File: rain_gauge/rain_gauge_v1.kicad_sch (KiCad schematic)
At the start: 16 parts, among them J1 Conn_01x05_Pin, SW1 SW_Reed, U1 S35770, U2 SN74LVC1G14DBV, U3 AP2112K-3.3

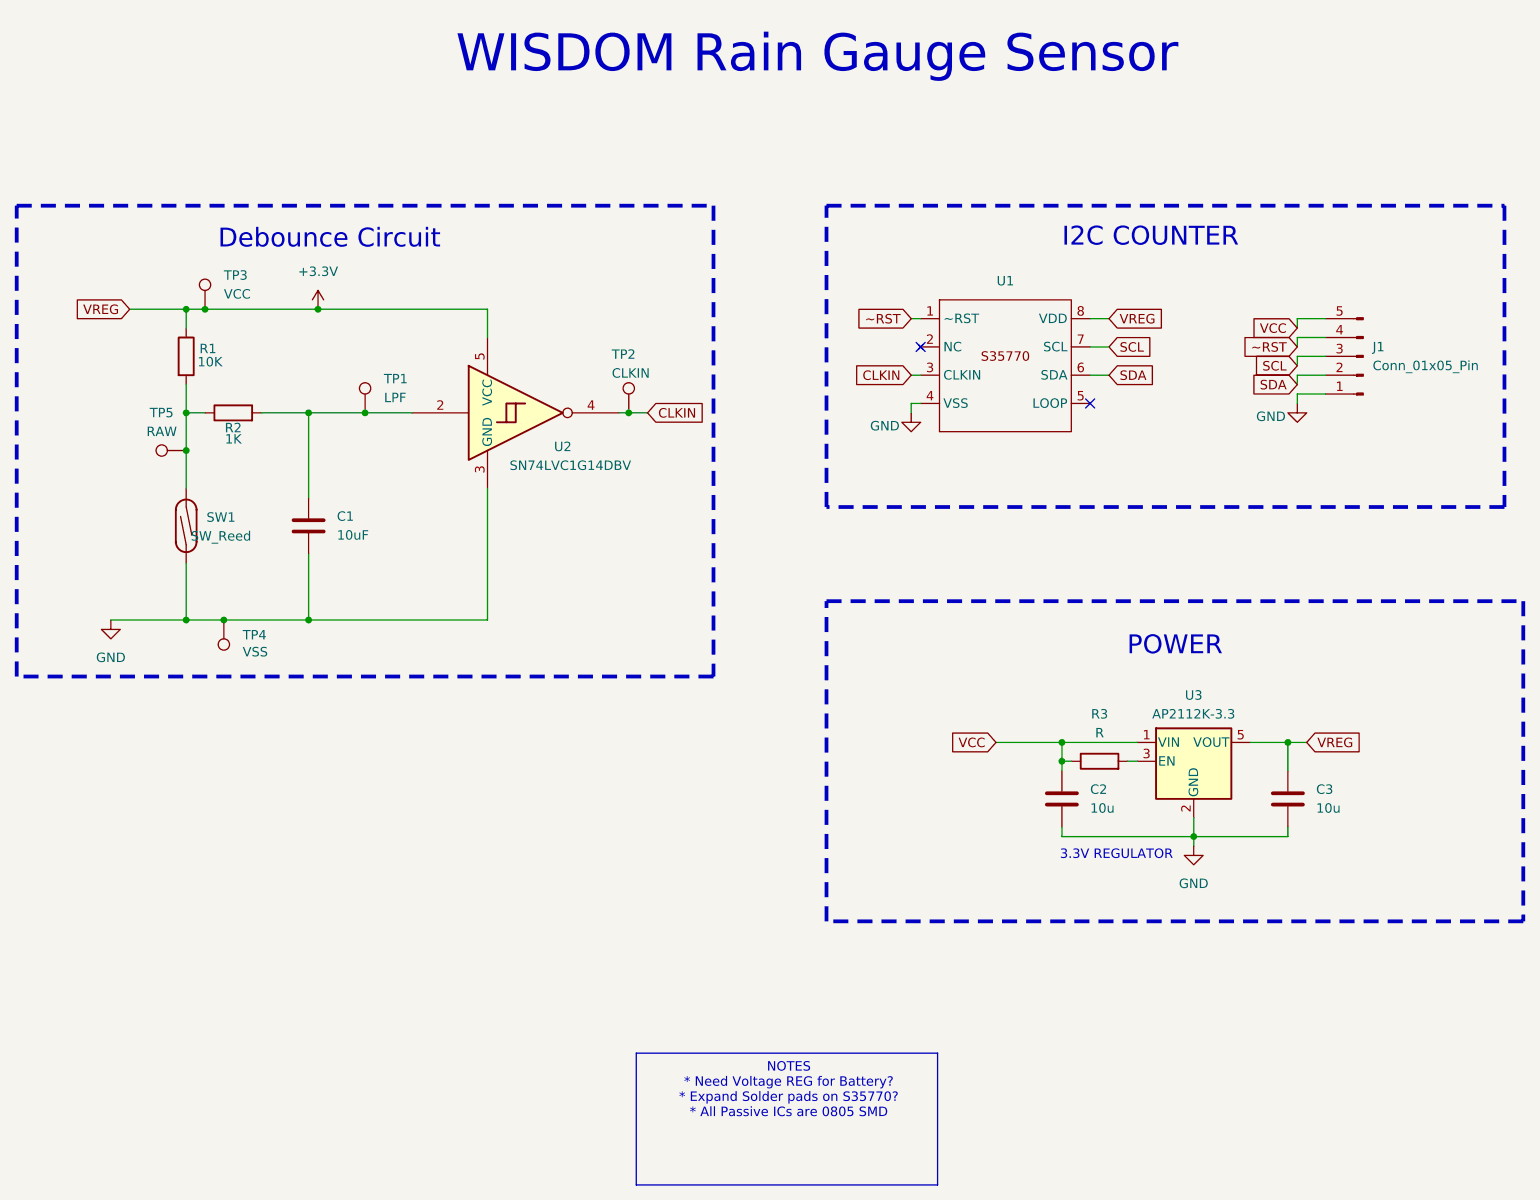
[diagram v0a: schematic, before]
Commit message: remove regulator, add decoupling, add pullups
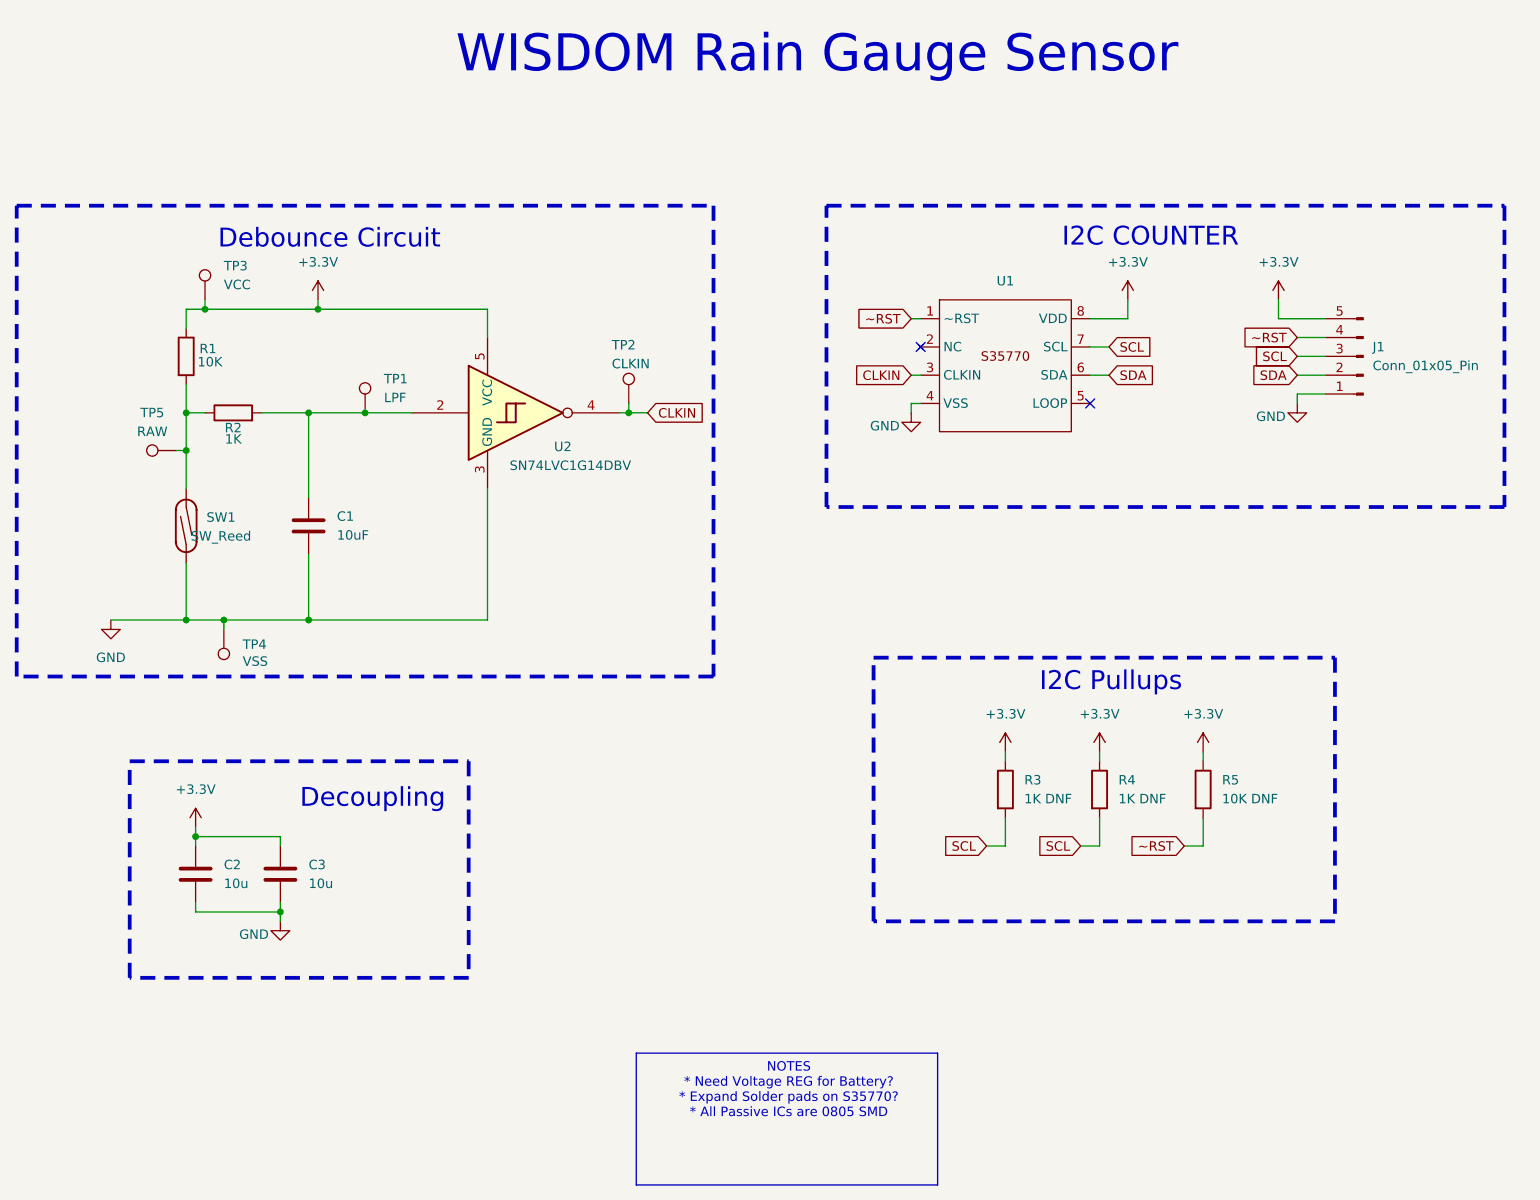
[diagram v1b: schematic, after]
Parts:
- removed U3: AP2112K-3.3, Package_TO_SOT_SMD:SOT-23-5, symbol Regulator_Linear:AP2112K-3.3
- added R4: 1K DNF, symbol Device:R
- added R5: 10K DNF, symbol Device:R
- C2, C3: footprint Capacitor_SMD:C_0805_2012Metric_Pad1.18x1.45mm_HandSolder -> (none)
- R3: value R -> 1K DNF; footprint Resistor_SMD:R_0805_2012Metric_Pad1.20x1.40mm_HandSolder -> (none)
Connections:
- net VCC is gone; now on net +3.3V: C2.1, J1.5 (Pin_5), R3.1
- net +3.3V: now also R4.1, R5.1
- net SCL: now also R3.2, R4.2
- net ~RST: now also R5.2
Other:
- note added: "Decoupling"
- note added: "I2C Pullups"
- note removed: "3.3V REGULATOR"
- note removed: "POWER"
- moved on the sheet: TP2, TP3, TP4, TP5

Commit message: Rain Gauge V2
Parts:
- C2, C3: footprint (none) -> Capacitor_SMD:C_0805_2012Metric_Pad1.18x1.45mm_HandSolder
- R3, R4, R5: footprint (none) -> Resistor_SMD:R_0805_2012Metric_Pad1.20x1.40mm_HandSolder
- U1: footprint Package_TMSOP:TMSOP8 -> WiSDOM:TMSOP08_2P9X2P8_ABL
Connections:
- net +3.3V: now also J1.2 (Pin_2); no longer J1.5 (Pin_5)
- net SCL: now also J1.5 (Pin_5); no longer J1.3 (Pin_3), R4.2
- net SDA: now also J1.4 (Pin_4), R4.2; no longer J1.2 (Pin_2)
- net ~RST: now also J1.3 (Pin_3); no longer J1.4 (Pin_4)
